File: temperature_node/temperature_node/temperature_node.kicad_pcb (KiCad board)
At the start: 4 copper layers, 23 x 24.5 mm, 35 parts, among them CN1 UART, J1 USB_C_Receptacle_USB2.0_16P, J2 S2B-PH-K-S, U1 SHT40-AD1B-R3, U2 MCP73831-2-OT, U3 MIC5504-3.3YM5, U4 ESP32-C3-WROOM-02, U6 USBLC6-2P6

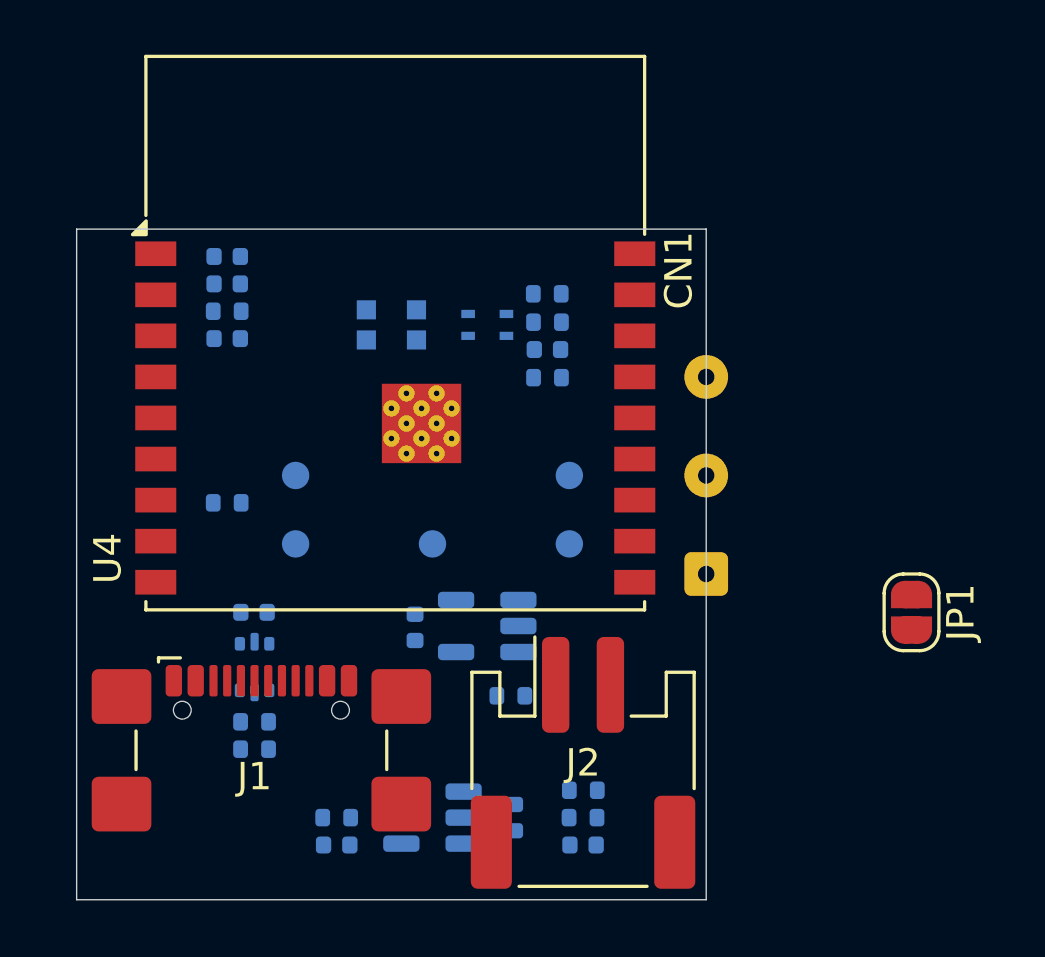
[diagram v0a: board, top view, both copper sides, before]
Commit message: Reorder connectors to shorter USB routing
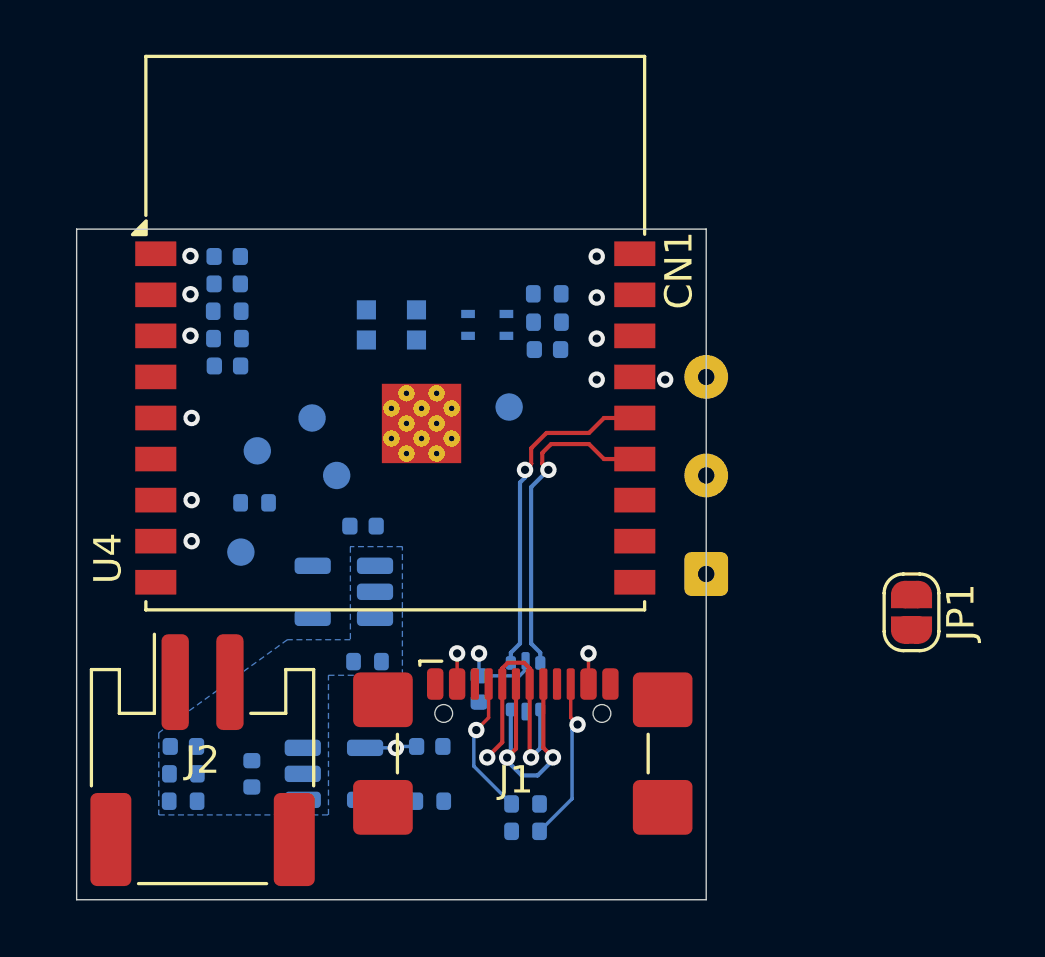
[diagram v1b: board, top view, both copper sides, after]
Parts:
- moved C3 15.0 mm to (124.9, 98.9), turned to 180 degrees
- moved R11 14.7 mm to (124.9, 99.9), turned to 180 degrees
- moved R12 14.6 mm to (124.9, 100.9), turned to 180 degrees
- moved J2 13.9 mm to (125.6, 99.4)
- moved TP2 12.0 mm to (127.0, 91.8)
- moved R8 12.0 mm to (126.5, 83.0)
- moved TP5 11.4 mm to (127.6, 88.1)
- moved R5 10.3 mm to (137.4, 101.0), turned to 180 degrees
- moved R6 10.3 mm to (137.4, 102.0)
- moved U6 9.92 mm to (137.4, 96.7)
- moved C4 9.73 mm to (127.4, 99.9), turned to -90 degrees
- moved J1 9.55 mm to (137.3, 100.3)
- moved TP1 9.26 mm to (136.8, 86.5)
- moved C9 8.68 mm to (135.7, 96.8), turned to -90 degrees
- moved TP4 6.37 mm to (129.6, 86.9)
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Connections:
- net Net-(J1-D+-PadA6) renamed /D_P
- net Net-(J1-D--PadA7) renamed /D_N
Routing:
- net /D+: track 0.00 -> 12.4 mm, vias 0 -> 1
- net /D-: track 0.00 -> 11.9 mm, vias 0 -> 1
- net /D_N: track 0.00 -> 9.87 mm, vias 0 -> 2
- net /D_P: track 0.00 -> 9.80 mm, vias 0 -> 2
- net VBUS: track 0.00 -> 7.08 mm, vias 0 -> 4
- net Net-(J1-CC2): track 0.00 -> 6.06 mm, vias 0 -> 1
- net Net-(J1-CC1): track 0.00 -> 5.18 mm, vias 0 -> 1
- net Net-(U2-PROG): track 0.00 -> 1.87 mm
- net Net-(U4-IO8): vias 0 -> 1
- net Net-(U4-IO2): vias 0 -> 1
- net Net-(JP1-B): vias 0 -> 1
- net /SHT_EN: vias 0 -> 1
- net /SDA: vias 0 -> 1
- net /SCL: vias 0 -> 1
- net /LED_DI: vias 0 -> 1
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- added copper zone on B.Cu, net +BATT
- added copper zone on In1.Cu, net VBUS

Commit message: PCB Routed pre DRC
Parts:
- removed JP1: ~, Jumper:SolderJumper-2_P1.3mm_Open_RoundedPad1.0x1.5mm
- added J3: IO9, Connector_Wire:SolderWire-0.1sqmm_1x02_P3.6mm_D0.4mm_OD1mm, F.Cu at (121.0, 81.4)
- moved TP5 20.9 mm to (142.4, 102.8)
- moved R4 9.08 mm to (124.9, 101.9)
- moved TP4 9.00 mm to (138.6, 86.9)
- moved TP1 8.32 mm to (139.7, 94.3)
- moved TP2 5.80 mm to (126.9, 97.6)
- moved C4 4.02 mm to (130.7, 97.6), turned to 0 degrees
- moved TP3 1.42 mm to (129.6, 87.9)
- moved R9 0.10 mm to (127.5, 89.9)
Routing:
- net /CHG_STAT: track 0.00 -> 27.9 mm, vias 0 -> 1
- net /BATT_Att: track 0.00 -> 24.9 mm
- net /SHT_EN: track 0.00 -> 23.7 mm
- net Net-(U4-IO2): track 0.00 -> 18.6 mm, vias 1 -> 3
- net Net-(J3-Pin_1): track 0.00 -> 12.8 mm
- net +3.3V: track 0.00 -> 12.2 mm, vias 1 -> 5
- net +BATT: track 0.00 -> 11.2 mm, vias 0 -> 7
- net /SCL: track 0.00 -> 9.19 mm
- net /LED_DI: track 0.00 -> 8.16 mm
- net GND: track 0.00 -> 7.01 mm
- net /SDA: track 0.00 -> 5.51 mm
- net /EN: track 0.00 -> 4.26 mm
- net Net-(U4-IO8): track 0.00 -> 3.10 mm
- net /D_N: track 9.87 -> 6.91 mm, vias 2 -> 1
- net /RX: track 0.00 -> 2.54 mm
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- added copper zone on In1.Cu, net +3.3V
- added copper zone on In1.Cu, net +BATT
- added copper zone on B.Cu, net GND
- added copper zone on F.Cu, net GND
- added copper zone on In2.Cu, net GND
- removed copper zone on B.Cu, net +BATT
